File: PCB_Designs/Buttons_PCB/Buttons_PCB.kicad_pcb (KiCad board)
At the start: 2 copper layers, 49.5 x 158.8 mm, 71 parts, among them P1 CONN_01X05, P2 CONN_01X01, P3 CONN_01X01, P4 CONN_01X01, U1 CHERRY-MX, U10 CHERRY-MX, U11 CHERRY-MX, U12 CHERRY-MX, U13 MCP23017, U14 MCP23017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

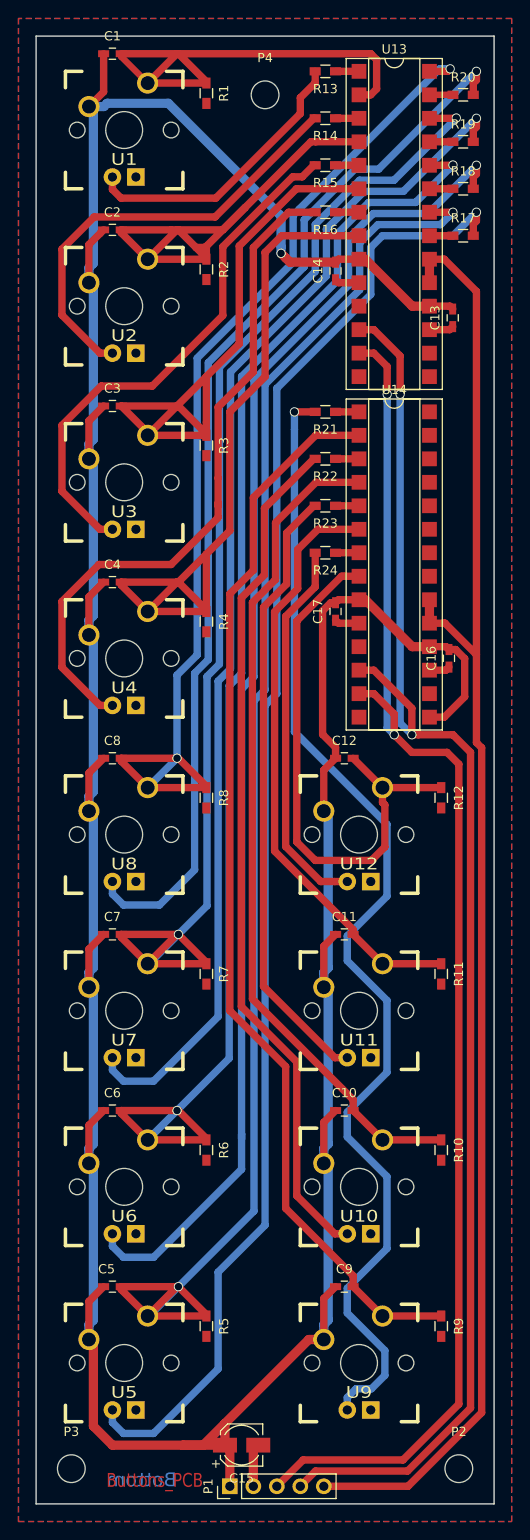
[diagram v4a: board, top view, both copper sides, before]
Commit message: Buttons V4
Pulldown changed to pullup in button switch filter.
Filter to switch completed (changed).
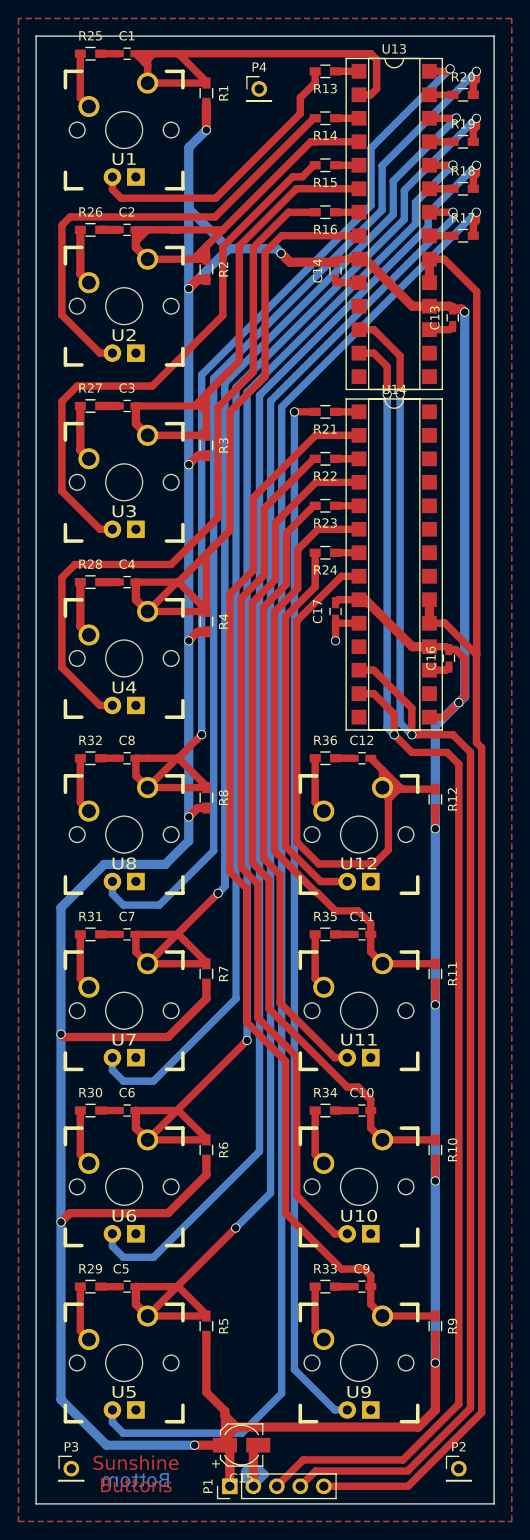
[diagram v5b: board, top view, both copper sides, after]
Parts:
- added R25: 220, Resistors_SMD:R_0603_HandSoldering, F.Cu at (70.0, 27.3)
- added R26: 220, Resistors_SMD:R_0603_HandSoldering, F.Cu at (70.0, 46.4)
- added R27: 220, Resistors_SMD:R_0603_HandSoldering, F.Cu at (70.0, 65.4)
- added R28: 220, Resistors_SMD:R_0603_HandSoldering, F.Cu at (70.0, 84.5)
- added R29: 220, Resistors_SMD:R_0603_HandSoldering, F.Cu at (70.0, 160.7)
- added R30: 220, Resistors_SMD:R_0603_HandSoldering, F.Cu at (70.0, 141.6)
- added R31: 220, Resistors_SMD:R_0603_HandSoldering, F.Cu at (70.0, 122.6)
- added R32: 220, Resistors_SMD:R_0603_HandSoldering, F.Cu at (70.0, 103.5)
- added R33: 220, Resistors_SMD:R_0603_HandSoldering, F.Cu at (95.4, 160.7)
- added R34: 220, Resistors_SMD:R_0603_HandSoldering, F.Cu at (95.4, 141.6)
- added R35: 220, Resistors_SMD:R_0603_HandSoldering, F.Cu at (95.4, 122.6)
- added R36: 220, Resistors_SMD:R_0603_HandSoldering, F.Cu at (95.4, 103.5)
- P2, P3, P4: footprint Mounting_Holes:MountingHole_3mm -> Socket_Strips:Socket_Strip_Straight_1x01_Pitch2.54mm
- moved C10 1.91 mm to (99.4, 141.6)
- moved C11 1.91 mm to (99.4, 122.6)
- moved C12 1.91 mm to (99.4, 103.5)
- moved C9 1.91 mm to (99.4, 160.7)
- moved C3 1.59 mm to (74.0, 65.4)
- moved C4 1.59 mm to (74.0, 84.5)
- moved C5 1.59 mm to (74.0, 160.7)
- moved C6 1.59 mm to (74.0, 141.6)
- moved C7 1.59 mm to (74.0, 122.6)
- moved C8 1.59 mm to (74.0, 103.5)
- moved C1 1.58 mm to (74.0, 27.3)
- moved C2 1.58 mm to (74.0, 46.4)
- moved P4 0.90 mm to (88.3, 31.1)
- moved R12 0.66 mm to (107.3, 108.0)
- moved R10 0.64 mm to (107.3, 145.9)
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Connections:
- C1 pad 1: /VDD -> /GND
- C10 pad 1: /VDD -> /GND
- C11 pad 1: /VDD -> /GND
- C12 pad 1: /VDD -> /GND
- C2 pad 1: /VDD -> /GND
- C3 pad 1: /VDD -> /GND
- C4 pad 1: /VDD -> /GND
- C5 pad 1: /VDD -> /GND
- C6 pad 1: /VDD -> /GND
- C7 pad 1: /VDD -> /GND
- C8 pad 1: /VDD -> /GND
- C9 pad 1: /VDD -> /GND
- R1 pad 2: /GND -> /VDD
- R10 pad 2: /GND -> /VDD
- R11 pad 2: /GND -> /VDD
- R12 pad 2: /GND -> /VDD
- R2 pad 2: /GND -> /VDD
- R3 pad 2: /GND -> /VDD
- R4 pad 2: /GND -> /VDD
- R5 pad 2: /GND -> /VDD
- R6 pad 2: /GND -> /VDD
- R7 pad 2: /GND -> /VDD
- R8 pad 2: /GND -> /VDD
- R9 pad 2: /GND -> /VDD
- U1 pad 2: /VDD -> Net-(R25-Pad1)
- U10 pad 2: /VDD -> Net-(R34-Pad1)
- U11 pad 2: /VDD -> Net-(R35-Pad1)
- U12 pad 2: /VDD -> Net-(R36-Pad1)
- U2 pad 2: /VDD -> Net-(R26-Pad1)
- U3 pad 2: /VDD -> Net-(R27-Pad1)
- U4 pad 2: /VDD -> Net-(R28-Pad1)
- U5 pad 2: /VDD -> Net-(R29-Pad1)
- U6 pad 2: /VDD -> Net-(R30-Pad1)
- U7 pad 2: /VDD -> Net-(R31-Pad1)
- U8 pad 2: /VDD -> Net-(R32-Pad1)
- U9 pad 2: /VDD -> Net-(R33-Pad1)
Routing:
- net /VDD: track 417.3 -> 459.9 mm, vias 1 -> 15
- net /GND: track 14.9 -> 46.4 mm, vias 0 -> 1
- net Net-(D9-Pad1): track 127.6 -> 113.4 mm
- net Net-(C2-Pad2): track 58.1 -> 47.0 mm
- net Net-(C5-Pad2): track 165.6 -> 155.1 mm
- net Net-(R30-Pad1): track 0.00 -> 6.78 mm
- net Net-(R32-Pad1): track 0.00 -> 6.78 mm
- net Net-(R26-Pad1): track 0.00 -> 6.78 mm
- net Net-(R35-Pad1): track 0.00 -> 6.78 mm
- net Net-(R28-Pad1): track 0.00 -> 6.78 mm
- net Net-(R25-Pad1): track 0.00 -> 6.78 mm
- net Net-(R31-Pad1): track 0.00 -> 6.78 mm
- net Net-(R29-Pad1): track 0.00 -> 6.78 mm
- net Net-(R27-Pad1): track 0.00 -> 6.78 mm
- net Net-(C7-Pad2): track 136.4 -> 129.8 mm
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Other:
- net class Default: trace_width 0.6 -> 0.7
- rule trace_min: 0.6 -> 0.7
- board text added: "Sunshine Buttons"
- board text removed: "Buttons_PCB"

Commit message: Main_PCB V1 Complete
Minor changes to everything.
Main_PCB complete with traces and design.
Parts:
- C15: footprint Capacitors_SMD:CP_Elec_4x4.5 -> Capacitors_Tantalum_SMD:CP_Tantalum_Case-A_EIA-3216-18_Reflow
- P1: value CONN_01X05 -> CONN_02X05; footprint Socket_Strips:Socket_Strip_Straight_1x05_Pitch2.54mm -> Connectors_Multicomp:Multicomp_MC9A22-1034_2x05x2.54mm_Angled; moved to B.Cu
- moved C15 3.81 mm to (86.4, 174.0)
- moved P1 3.18 mm to (85.1, 179.1), turned to 0 degrees
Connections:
- P1 pad 2: /GND -> /VDD
- P1 pad 3: /S_DAT_L -> /GND
- P1 pad 4: /S_CLK_L -> /GND
- P1 pad 5: /intA -> /S_DAT_L
- P2 pad 1: (no net) -> Net-(P2-Pad1)
- P3 pad 1: (no net) -> Net-(P3-Pad1)
- P4 pad 1: (no net) -> Net-(P4-Pad1)
- U13 pad 19: /intA -> /INT
- U13 pad 20: /intA -> /INT
- U14 pad 19: /intA -> /INT
- U14 pad 20: /intA -> /INT
- U14 pad 21: (no net) -> Net-(U14-Pad21)
- U14 pad 22: (no net) -> Net-(U14-Pad22)
- U14 pad 23: (no net) -> Net-(U14-Pad23)
- U14 pad 24: (no net) -> Net-(U14-Pad24)
- U14 pad 25: (no net) -> Net-(U14-Pad25)
- U14 pad 26: (no net) -> Net-(U14-Pad26)
- U14 pad 27: (no net) -> Net-(U14-Pad27)
- U14 pad 28: (no net) -> Net-(U14-Pad28)
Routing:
- net /INT: track 0.00 -> 163.8 mm
- net /intA: track 160.0 -> 0.00 mm
- net /GND: track 46.4 -> 63.7 mm, vias 1 -> 3
- net /S_CLK_L: track 157.4 -> 162.8 mm
- net /S_DAT_L: track 151.6 -> 155.5 mm
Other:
- board size 49.5 x 158.8 mm -> 49.9 x 158.8 mm

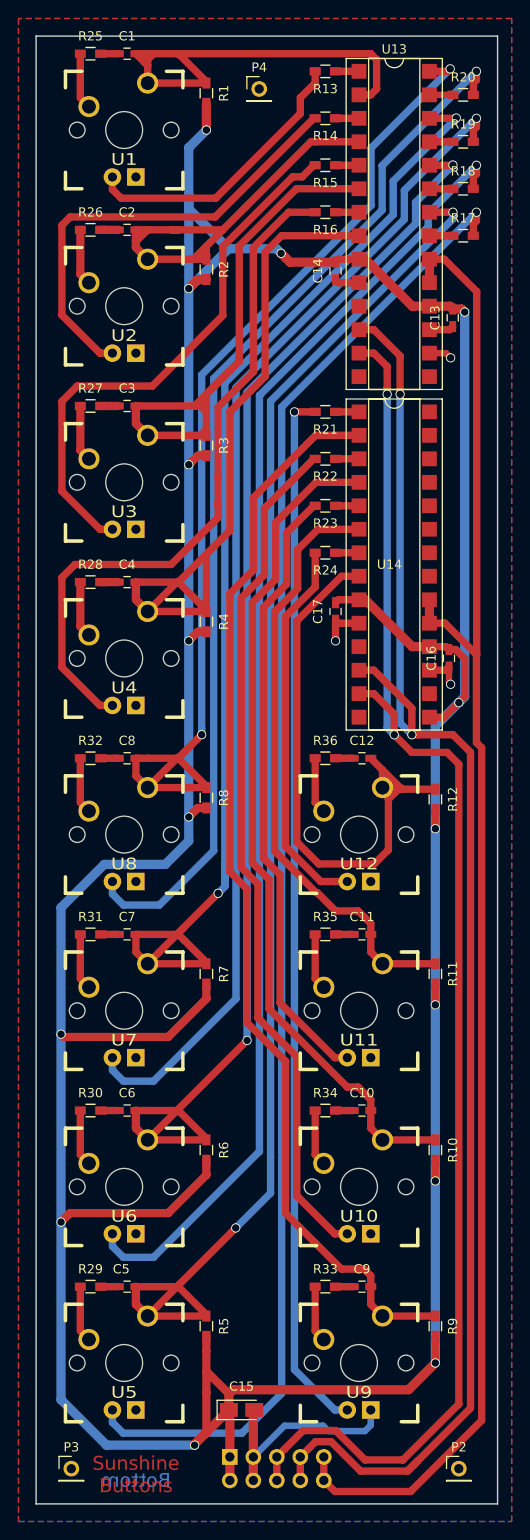
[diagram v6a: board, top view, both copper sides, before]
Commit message: Completed all Circuits for evaluation
* All board-to-board connectors now Multicomp 02X05
* Mounting holes for all PCB
* Vias at all groundpins
* Minor other changes
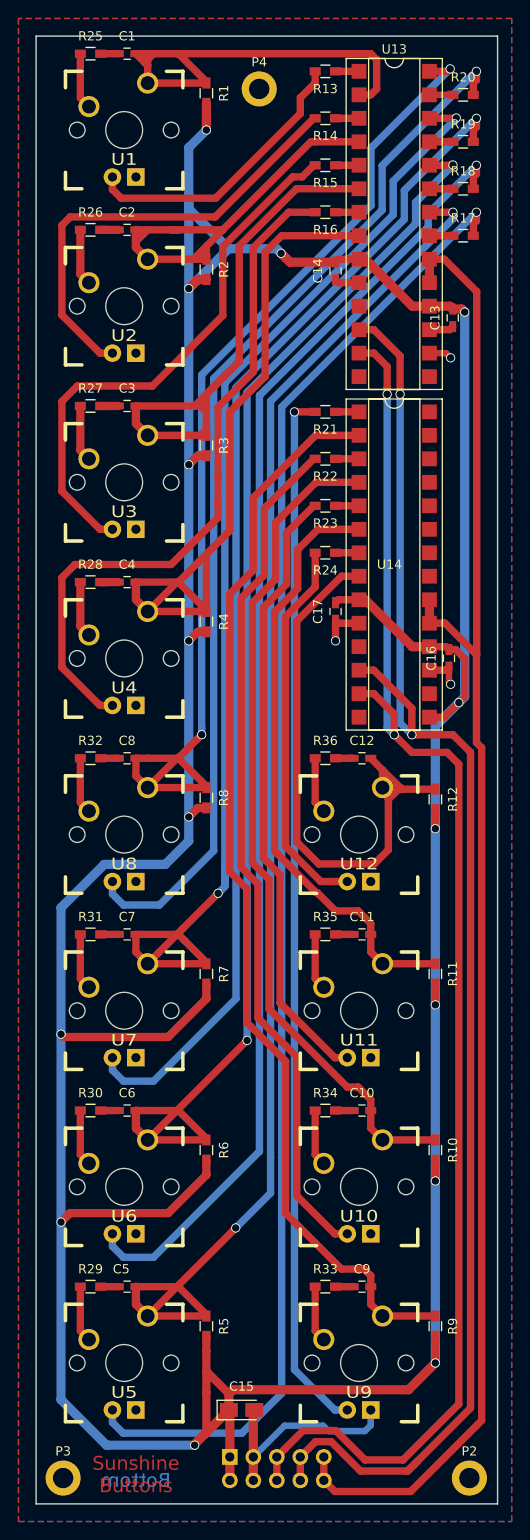
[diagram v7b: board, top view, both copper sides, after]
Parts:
- P2, P3, P4: footprint Socket_Strips:Socket_Strip_Straight_1x01_Pitch2.54mm -> Mounting_Holes:MountingHole_2.2mm_M2_DIN965_Pad
- moved P2 1.53 mm to (111.0, 181.4)
- moved P3 1.35 mm to (67.1, 181.4)
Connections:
- P2 pad 1: Net-(P2-Pad1) -> (no net)
- P3 pad 1: Net-(P3-Pad1) -> (no net)
- P4 pad 1: Net-(P4-Pad1) -> (no net)
- U14 pad 21: Net-(U14-Pad21) -> (no net)
- U14 pad 22: Net-(U14-Pad22) -> (no net)
- U14 pad 23: Net-(U14-Pad23) -> (no net)
- U14 pad 24: Net-(U14-Pad24) -> (no net)
- U14 pad 25: Net-(U14-Pad25) -> (no net)
- U14 pad 26: Net-(U14-Pad26) -> (no net)
- U14 pad 27: Net-(U14-Pad27) -> (no net)
- U14 pad 28: Net-(U14-Pad28) -> (no net)

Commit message: Buttons wrong IO expander footprint fixed
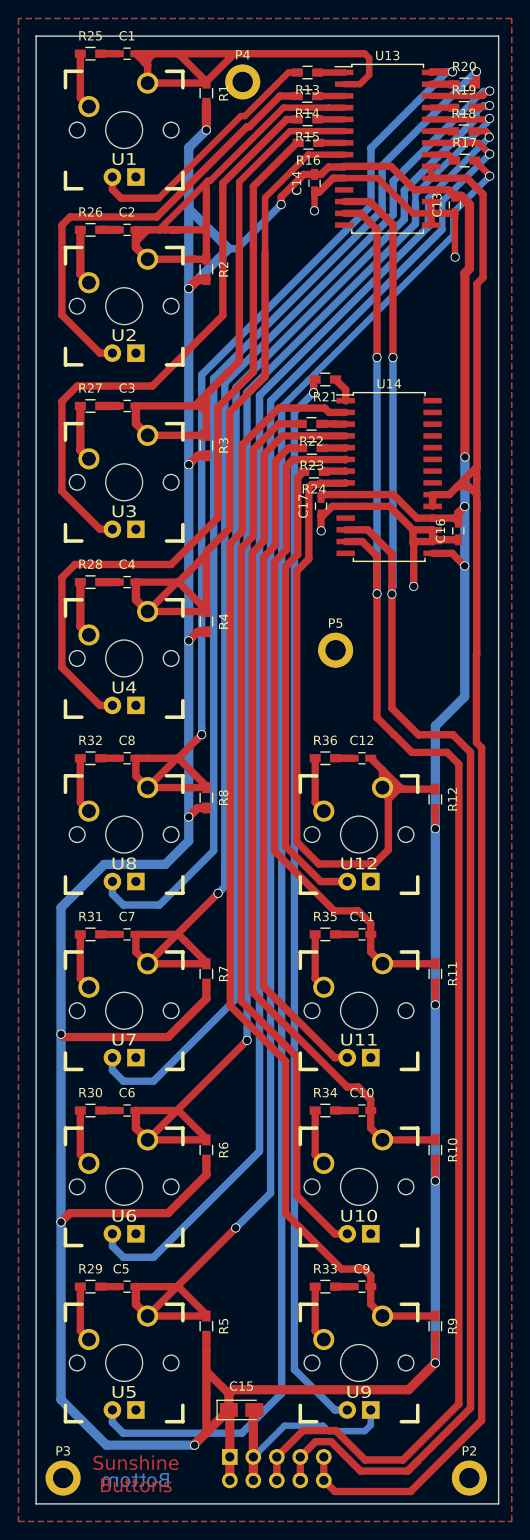
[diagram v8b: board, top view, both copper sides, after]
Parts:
- added P5: CONN_01X01, Mounting_Holes:MountingHole_2.2mm_M2_DIN965_Pad, F.Cu at (96.5, 91.8)
- U13, U14: footprint Housings_DIP:DIP-28_W7.62mm_SMDSocket_SmallPads -> Housings_SOIC:SOIC-28W_7.5x17.9mm_Pitch1.27mm
- moved C16 13.8 mm to (109.8, 78.9)
- moved C13 12.2 mm to (109.4, 43.7)
- moved C17 11.5 mm to (95.0, 76.2)
- moved C14 9.76 mm to (94.2, 41.3)
- moved U14 9.48 mm to (102.3, 73.1)
- moved R24 8.86 mm to (94.2, 72.5)
- moved U13 8.17 mm to (102.2, 37.6)
- moved R17 8.13 mm to (110.5, 38.9)
- moved R16 7.72 mm to (93.6, 37.0)
- moved R23 6.42 mm to (94.0, 70.0)
- moved R18 6.22 mm to (110.4, 35.7)
- moved R15 5.32 mm to (93.5, 34.4)
- moved R22 4.07 mm to (93.9, 67.3)
- moved R19 3.68 mm to (110.4, 33.1)
- moved R21 3.50 mm to (95.4, 62.5)
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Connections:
- P2 pad 1: (no net) -> Net-(P2-Pad1)
- P3 pad 1: (no net) -> Net-(P3-Pad1)
- P4 pad 1: (no net) -> Net-(P4-Pad1)
- U14 pad 21: (no net) -> Net-(U14-Pad21)
- U14 pad 22: (no net) -> Net-(U14-Pad22)
- U14 pad 23: (no net) -> Net-(U14-Pad23)
- U14 pad 24: (no net) -> Net-(U14-Pad24)
- U14 pad 25: (no net) -> Net-(U14-Pad25)
- U14 pad 26: (no net) -> Net-(U14-Pad26)
- U14 pad 27: (no net) -> Net-(U14-Pad27)
- U14 pad 28: (no net) -> Net-(U14-Pad28)
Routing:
- net /GND: track 63.7 -> 101.2 mm, vias 3 -> 4
- net /S_DAT_L: track 155.5 -> 172.6 mm
- net /S_CLK_L: track 162.8 -> 177.8 mm
- net Net-(C5-Pad2): track 155.1 -> 167.3 mm
- net /VDD: track 459.9 -> 471.7 mm, vias 15 -> 16
- net /INT: track 163.8 -> 174.8 mm
- net Net-(C2-Pad2): track 47.0 -> 57.9 mm
- net Net-(C6-Pad2): track 140.7 -> 151.2 mm
- net Net-(C12-Pad2): track 65.1 -> 75.6 mm
- net Net-(C7-Pad2): track 129.8 -> 138.3 mm
- net Net-(D12-Pad1): track 41.3 -> 49.6 mm
- net Net-(C11-Pad2): track 65.4 -> 73.2 mm
- net Net-(D11-Pad1): track 66.6 -> 73.0 mm
- net Net-(C10-Pad2): track 90.9 -> 96.6 mm
- net Net-(C4-Pad2): track 80.2 -> 85.7 mm
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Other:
- board size 49.9 x 158.8 mm -> 50 x 158.8 mm
